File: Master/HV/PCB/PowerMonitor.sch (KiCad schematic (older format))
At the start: 100 parts, among them U1 AMC1302, U10 SN6501DBV, U12 AMC1301, U13 AMC1301, U15 OPA2197IDR, U16 ISL28022, U3 TPS76350, U4 SN6501DBV, U5 SFH617A-2X009T, U6 TPS76350

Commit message: maintenance update
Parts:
- C1, C17, C19, C2: footprint Capacitors_SMD:C_0805_HandSoldering -> Capacitor_SMD:C_0805_2012Metric
- C10, C11, C12, C13, C14, C15, C16, C18, C21, C22, C3, C4, C49, C5, C50, C52, C53, C58, C59, C62, C63, C65, C66, C68, C69, C71, C72, C73, C75, C9: footprint Capacitors_SMD:C_0603_HandSoldering -> Capacitor_SMD:C_0603_1608Metric
- D16, D5: footprint LEDs:LED_0603_HandSoldering -> LED_SMD:LED_0603_1608Metric
- R10: footprint Resistors_SMD:R_2512 -> Resistor_SMD:R_2512_6332Metric
- R119, R120, R122, R123, R125, R126, R19, R20: footprint Resistors_SMD:R_1206 -> Resistor_SMD:R_1206_3216Metric
- R129, R13, R130, R132, R133, R14, R142, R143, R144, R145, R148, R149, R15, R150, R151, R155, R156, R157, R158, R16, R160, R161, R164, R165, R166, R167, R17, R21, R22, R26, R30, R31, R35, R38, R39, R40, R43: footprint Resistors_SMD:R_0603_HandSoldering -> Resistor_SMD:R_0603_1608Metric
- R9: footprint Resistor_SMD:R_2512_6332Metric_Pad1.49x3.40mm_HandSolder -> Resistor_SMD:R_2512_6332Metric
- U10, U3, U4, U6: footprint TO_SOT_Packages_SMD:SOT-23-5_HandSoldering -> Package_TO_SOT_SMD:SOT-23-5

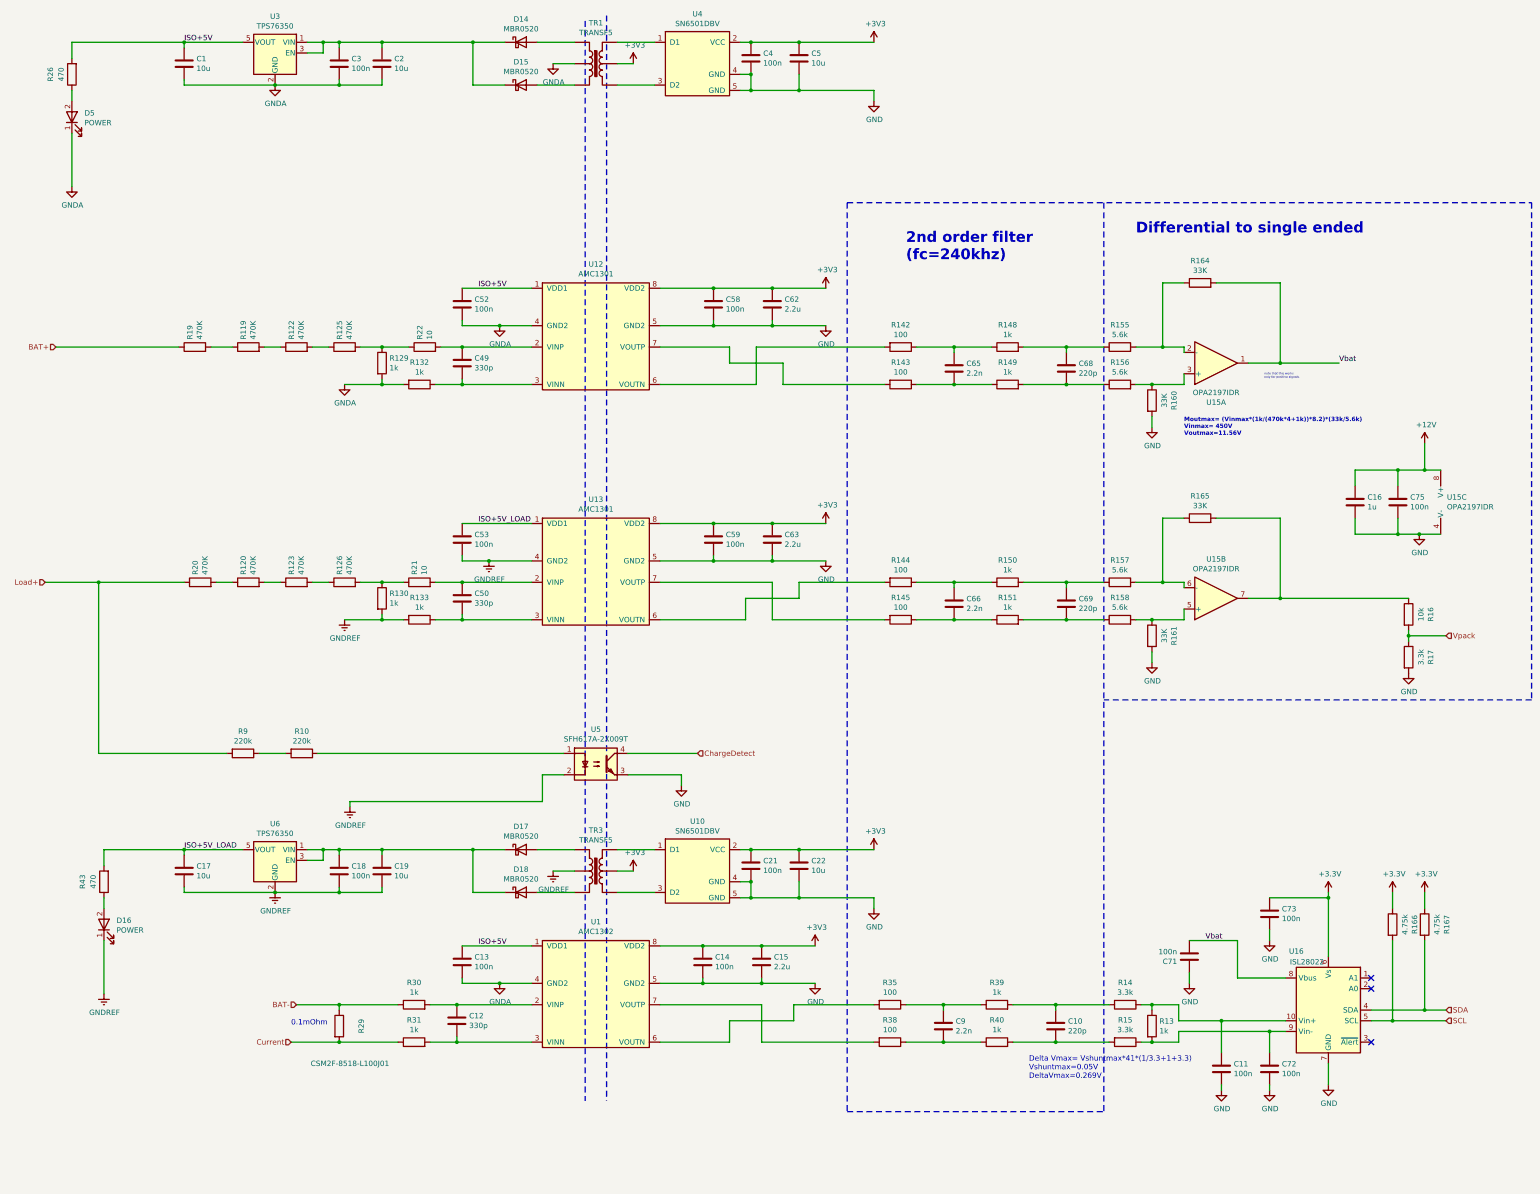
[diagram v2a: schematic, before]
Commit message: New parts for precharge circuit
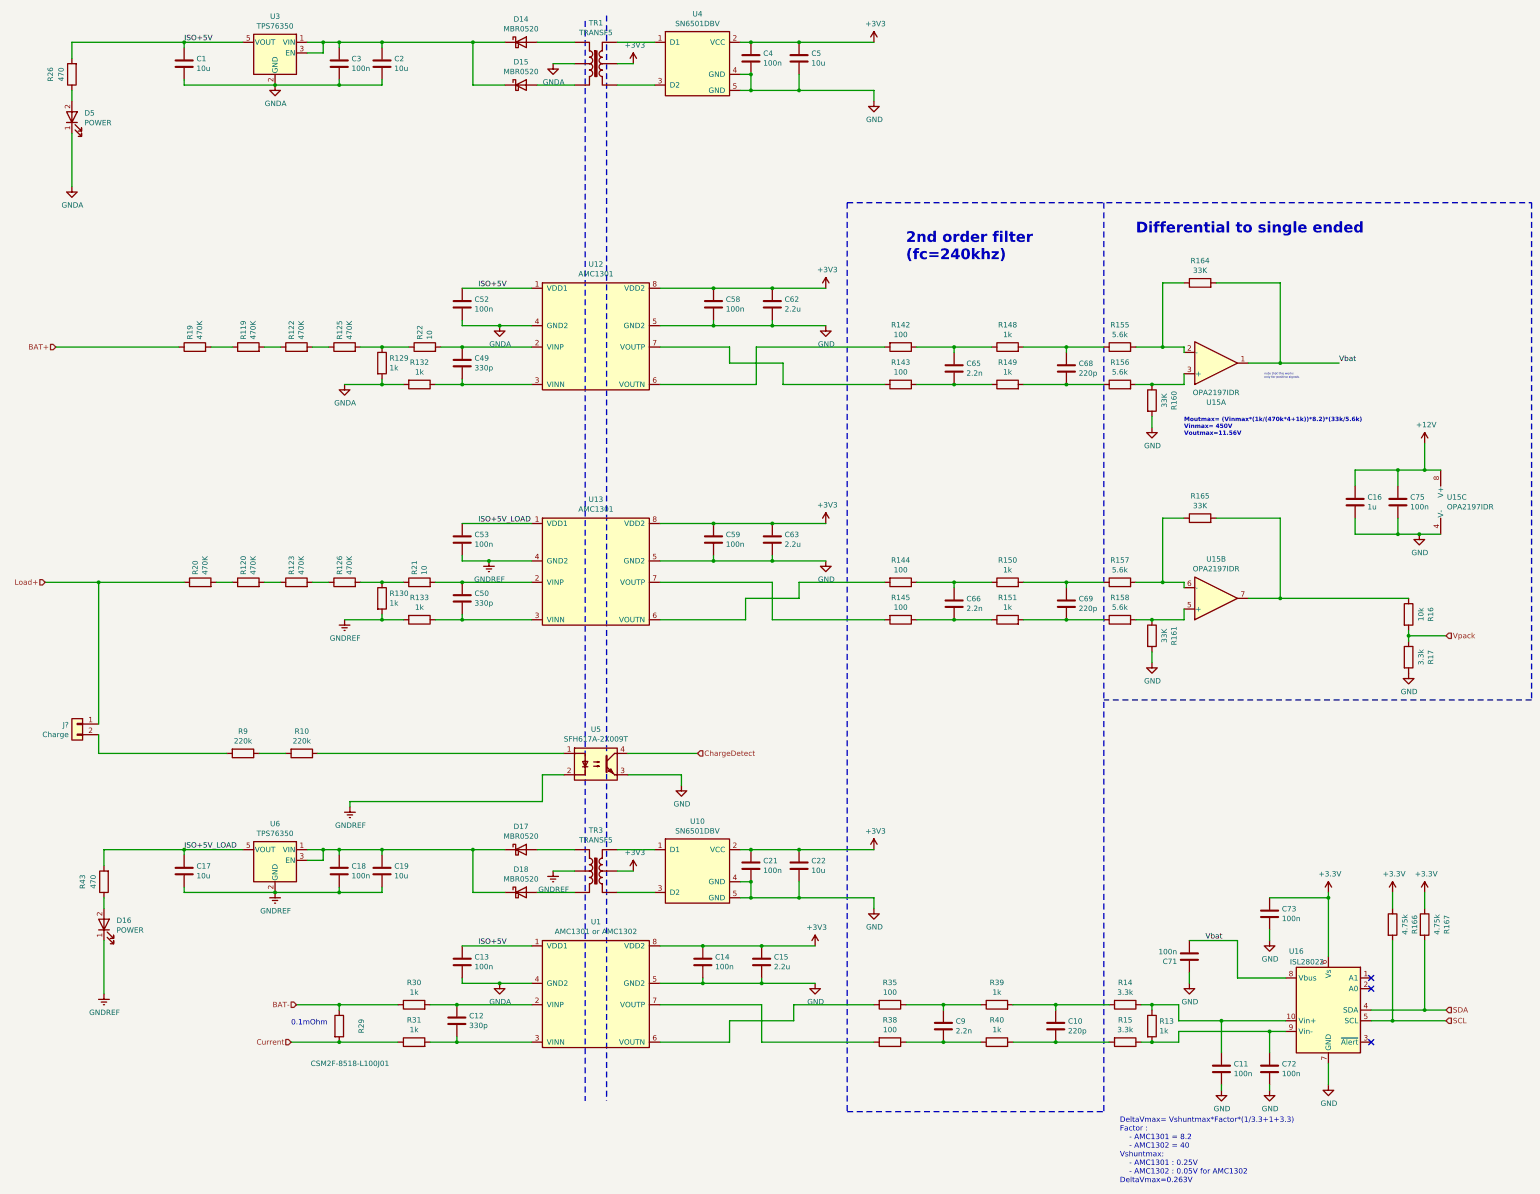
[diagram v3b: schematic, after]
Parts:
- added J?: Charge, Connector_Phoenix_GMSTB:PhoenixContact_GMSTBVA_2,5_2-G_1x02_P7.50mm_Vertical, symbol BMS-Master-rescue:Conn_01x02-Connector_Generic-BMS-Master-rescue
- U1: value AMC1302 -> AMC1301 or AMC1302; MPN AMC1302DWVR -> AMC1301DWV
- U5: footprint Housings_DIP:SMDIP-4_W7.62mm -> Housings_DIP:SMDIP-4_W9.53mm_Clearance8mm
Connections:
- net Load+: now also J?.1 (Pin_1); no longer R9.2
- new net: J?.2 (Pin_2), R9.2
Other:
- note added: "DeltaVmax= Vshuntmax*Factor*(1/3.3+1+3.3)\nFactor : \n - AMC1301 = 8.2\n - AMC1302 = 40\nVshuntmax:\n - AMC1301 : 0.25V \n - AMC1302 : 0.05V for AMC1302\nDeltaVmax=0.263V"
- note removed: "Delta Vmax= Vshuntmax*41*(1/3.3+1+3.3)\nVshuntmax=0.05V\nDeltaVmax=0.269V"
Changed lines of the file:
@@
 $EndComp
-Wire Wire Line
-	4650 6100 5150 6100
 Wire Wire Line
 	6700 6100 6850 6100
@@
 F 0 "U5" H 9800 8125 50  0000 C CNN
 F 1 "SFH617A-2X009T" H 9800 8034 50  0000 C CNN
-F 2 "Housings_DIP:SMDIP-4_W7.62mm" H 9800 7500 50  0001 C CNN
+F 2 "Housings_DIP:SMDIP-4_W9.53mm_Clearance8mm" H 9800 7500 50  0001 C CNN
 F 3 "http://www.vishay.com/docs/83740/sfh617a.pdf" H 9450 8100 50  0001 C CNN
 F 4 "SFH617A-2X009T" H 9800 7800 50  0001 C CNN "MPN"
@@
 	12150 2550 18550 2550
 Wire Wire Line
-	5150 7700 5150 6100
-Wire Wire Line
 	5150 7700 6350 7700
-Connection ~ 5150 6100
-Wire Wire Line
-	5150 6100 5950 6100
 $Comp
 L power:GND #PWR0209
@@
 P 9800 9950
 F 0 "U1" H 9800 10625 50  0000 C CNN
-F 1 "AMC1302" H 9800 10534 50  0000 C CNN
+F 1 "AMC1301 or AMC1302" H 9800 10534 50  0000 C CNN
 F 2 "Housings_SOIC:SSO-8_6.8x5.9mm_Pitch1.27mm_Clearance8mm" H 9800 9950 50  0001 C CNN
 F 3 "" H 9800 9950 50  0001 C CNN
-F 4 "AMC1302DWVR" H 9800 9950 50  0001 C CNN "MPN"
+F 4 "AMC1301DWV" H 9800 9950 50  0001 C CNN "MPN"
 	1    9800 9950
 	1    0    0    -1
@@
 	0    1    1    0
 $EndComp
-Text Notes 13850 10750 0    50   ~ 0
-Delta Vmax= Vshuntmax*41*(1/3.3+1+3.3)\nVshuntmax=0.05V\nDeltaVmax=0.269V
+Text Notes 14700 11725 0    50   ~ 0
+DeltaVmax= Vshuntmax*Factor*(1/3.3+1+3.3)\nFactor : \n	- AMC1301 = 8.2\n	- AMC1302 = 40\nVshuntmax:\n	- AMC1301 : 0.25V \n	- AMC1302 : 0.05V for AMC1302\nDeltaVmax=0.263V
 $Comp
 L Device:R R15
@@
 Wire Wire Line
 	8800 5900 9200 5900
+$Comp
+L BMS-Master-rescue:Conn_01x02-Connector_Generic-BMS-Master-rescue J?
+U 1 1 5E82887C
+P 4950 7425
+F 0 "J?" H 5029 7417 50  0000 L CNN
+F 1 "Charge" H 5029 7326 50  0000 L CNN
+F 2 "Connector_Phoenix_GMSTB:PhoenixContact_GMSTBVA_2,5_2-G_1x02_P7.50mm_Vertical" H 4950 7425 50  0001 C CNN
+F 3 "~" H 4950 7425 50  0001 C CNN
+F 4 "30.102 " H 4950 7425 50  0001 C CNN "MPN"
+	1    4950 7425
+	-1   0    0    -1
+$EndComp
+Wire Wire Line
+	4650 6100 5150 6100
+Wire Wire Line
+	5150 7425 5150 6100
+Connection ~ 5150 6100
+Wire Wire Line
+	5150 6100 5950 6100
+Wire Wire Line
+	5150 7525 5150 7700
 $EndSCHEMATC

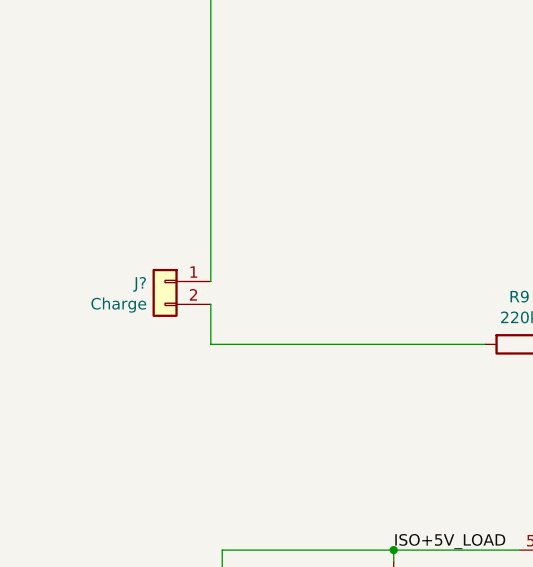
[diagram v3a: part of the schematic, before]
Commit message: Schematic Master-HV minor change
DischargeNeg has been switched to precharge for better code compatibility
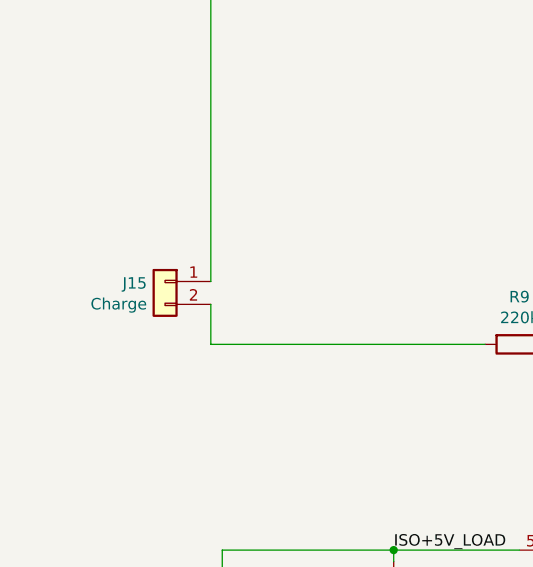
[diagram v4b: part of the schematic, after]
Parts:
- gave numbers to parts that had none: 1
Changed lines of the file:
@@
 	8800 5900 9200 5900
 $Comp
-L BMS-Master-rescue:Conn_01x02-Connector_Generic-BMS-Master-rescue J?
+L BMS-Master-rescue:Conn_01x02-Connector_Generic-BMS-Master-rescue J15
 U 1 1 5E82887C
 P 4950 7425
-F 0 "J?" H 5029 7417 50  0000 L CNN
+F 0 "J15" H 5029 7417 50  0000 L CNN
 F 1 "Charge" H 5029 7326 50  0000 L CNN
 F 2 "Connector_Phoenix_GMSTB:PhoenixContact_GMSTBVA_2,5_2-G_1x02_P7.50mm_Vertical" H 4950 7425 50  0001 C CNN

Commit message: Readme update
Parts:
- J15: value Charge -> Charge +
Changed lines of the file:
@@
 P 4950 7425
 F 0 "J15" H 5029 7417 50  0000 L CNN
-F 1 "Charge" H 5029 7326 50  0000 L CNN
+F 1 "Charge +" H 5029 7326 50  0000 L CNN
 F 2 "Connector_Phoenix_GMSTB:PhoenixContact_GMSTBVA_2,5_2-G_1x02_P7.50mm_Vertical" H 4950 7425 50  0001 C CNN
 F 3 "~" H 4950 7425 50  0001 C CNN
